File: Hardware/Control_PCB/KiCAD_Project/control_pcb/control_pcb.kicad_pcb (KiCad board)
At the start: 4 copper layers, 82.6 x 76.2 mm, 85 parts, among them J1 Conn_01x02, J2 ISP, J3 Spare 2, J5 Micro_SD_Card_Det, J6 Battery, J7 External Switch, Q1 BSS138, SW1 Freq Select, U1 STM32F103CBT6, U2 SN74LVC1G18, U3 TX2M-400-5-NSSL, U4 IF-D96F, U5 TC4S584F, U6 MAX-M8C, U7 LT1521-3.3, U8 MAX3232, Y1 8MHz

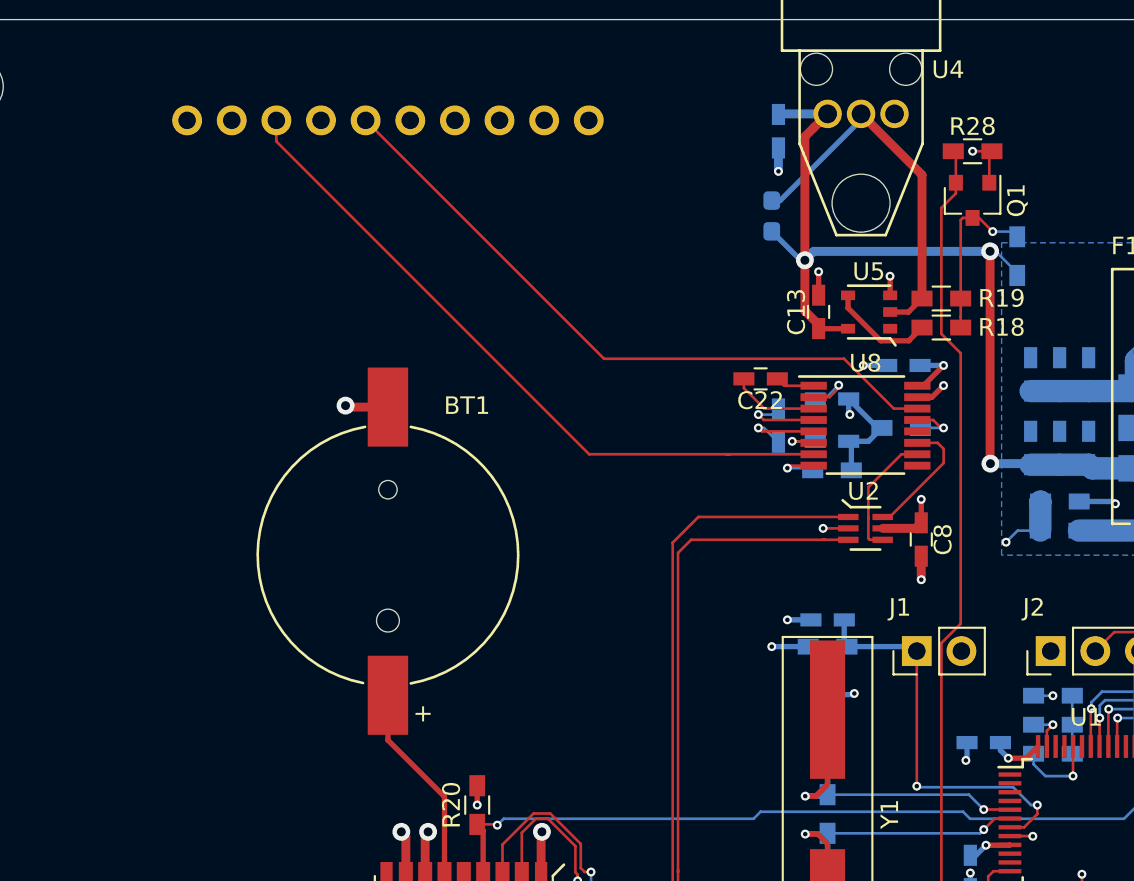
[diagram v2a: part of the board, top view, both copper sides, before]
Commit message: Fix TX2M footprint. Closes #2
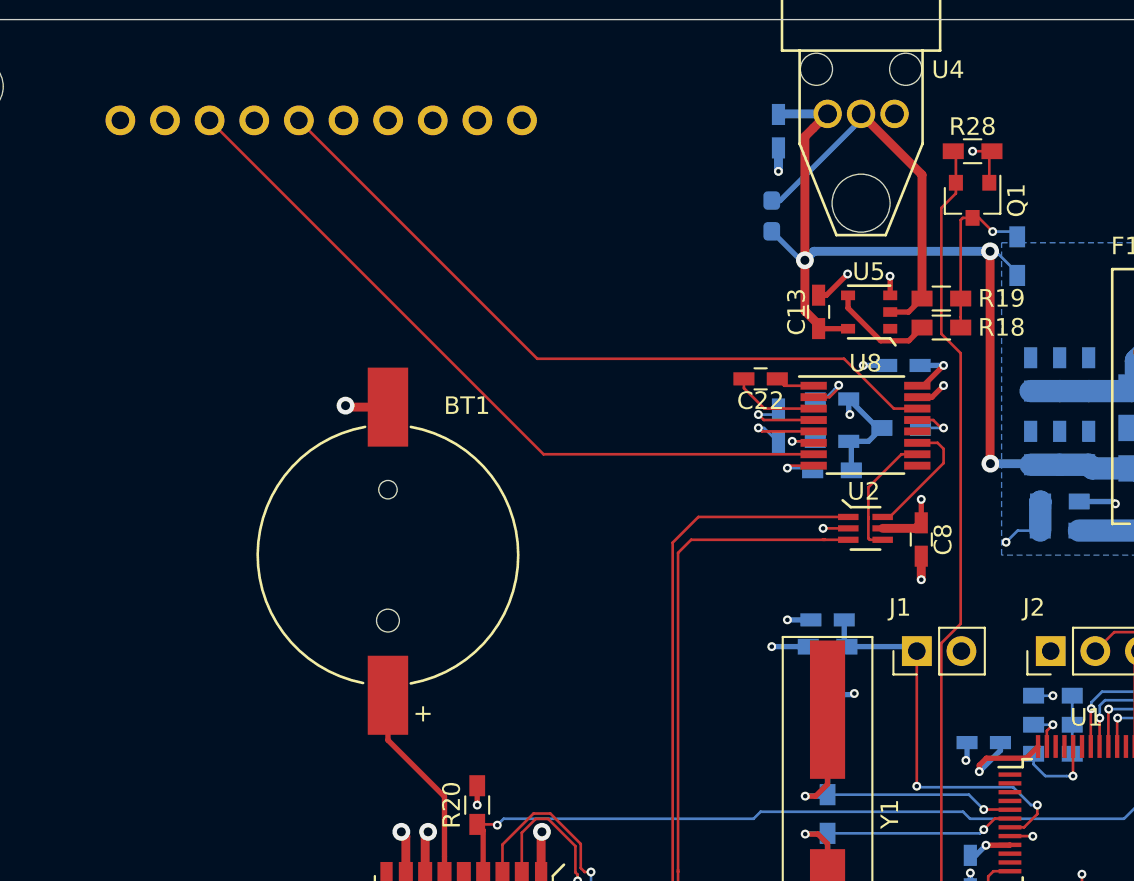
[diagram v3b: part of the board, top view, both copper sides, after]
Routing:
- net /radio/Programming_RS232: track 38.2 -> 42.0 mm
- net +3V3: track 64.8 -> 68.0 mm
- net /radio/Data_RS232: track 39.4 -> 42.2 mm
- net GND: track 66.2 -> 67.0 mm
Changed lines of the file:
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@@
     (thickness 1.6)
     (drawings 8)
-    (tracks 659)
+    (tracks 660)
     (zones 0)
     (modules 85)
@@
     (add_net TX_to_Radio)
   )
+  (module lib_fp:TX2M (layer B.Cu)
+    (at 100.965 128.905 90)
+    (fp_text reference U3 (at 24.257 -20.32 90) (layer B.SilkS)
+      (effects (font (size 1 1) (thickness 0.15)) (justify mirror))
+    )
+    (fp_text value TX2M-400-5-NSSL (at 0 0 90) (layer B.Fab)
+      (effects (font (size 1 1) (thickness 0.15)) (justify mirror))
+    )
+    (fp_line (start -30 -19.5) (end -30 19.5) (layer B.SilkS) (width 0.1))
+    (fp_line (start 30 -19.5) (end -30 -19.5) (layer B.SilkS) (width 0.1))
+    (fp_line (start 30 19.5) (end 30 -19.5) (layer B.SilkS) (width 0.1))
+    (fp_line (start -30 19.5) (end 30 19.5) (layer B.SilkS) (width 0.1))
+    (pad 8C thru_hole circle (at 26.65 -10.15 90) (size 1.7 1.7) (drill 1) (layers *.Cu *.Mask)
+      (net 51 /radio/Data_RS232))
+    (pad 2B thru_hole circle (at -24.11 -16.5 90) (size 1.7 1.7) (drill 1) (layers *.Cu *.Mask)
+      (net 1 "Net-(AE1-Pad1)"))
+    (pad 10C thru_hole circle (at 26.65 -15.23 90) (size 1.7 1.7) (drill 1) (layers *.Cu *.Mask))
+    (pad 9C thru_hole circle (at 26.65 -12.69 90) (size 1.7 1.7) (drill 1) (layers *.Cu *.Mask))
+    (pad 5C thru_hole circle (at 26.65 -2.53 90) (size 1.7 1.7) (drill 1) (layers *.Cu *.Mask))
+    (pad 3B thru_hole circle (at -26.65 -16.5 90) (size 1.7 1.7) (drill 1) (layers *.Cu *.Mask)
+      (net 2 GND))
+    (pad 1B thru_hole circle (at -21.57 -16.5 90) (size 1.7 1.7) (drill 1) (layers *.Cu *.Mask)
+      (net 2 GND))
+    (pad 2A thru_hole circle (at -26.65 16.5 90) (size 1.7 1.7) (drill 1) (layers *.Cu *.Mask)
+      (net 2 GND))
+    (pad 7C thru_hole circle (at 26.65 -7.61 90) (size 1.7 1.7) (drill 1) (layers *.Cu *.Mask)
+      (net 2 GND))
+    (pad 2C thru_hole circle (at 26.65 5.09 90) (size 1.7 1.7) (drill 1) (layers *.Cu *.Mask)
+      (net 2 GND))
+    (pad 1C thru_hole circle (at 26.65 7.63 90) (size 1.7 1.7) (drill 1) (layers *.Cu *.Mask)
+      (net 2 GND))
+    (pad 6C thru_hole circle (at 26.65 -5.07 90) (size 1.7 1.7) (drill 1) (layers *.Cu *.Mask)
+      (net 50 /radio/Programming_RS232))
+    (pad 4C thru_hole circle (at 26.65 0.01 90) (size 1.7 1.7) (drill 1) (layers *.Cu *.Mask))
+    (pad 3C thru_hole circle (at 26.65 2.55 90) (size 1.7 1.7) (drill 1) (layers *.Cu *.Mask))
+    (pad 1A thru_hole circle (at -24.11 16.5 90) (size 1.7 1.7) (drill 1) (layers *.Cu *.Mask)
+      (net 9 +BATT))
+  )
   (module lib_fp:SMA (layer F.Cu)
     (at 87.884 165.735)
@@
       (net 38 Radio_Serial_Select))
   )
-  (module lib_fp:TX2M (layer B.Cu)
-    (at 100.965 128.905 90)
-    (fp_text reference U3 (at 24.257 -20.32 90) (layer B.SilkS)
-      (effects (font (size 1 1) (thickness 0.15)) (justify mirror))
-    )
-    (fp_text value TX2M-400-5-NSSL (at 0 0 90) (layer B.Fab)
-      (effects (font (size 1 1) (thickness 0.15)) (justify mirror))
-    )
-    (fp_line (start -30 19.5) (end 30 19.5) (layer B.SilkS) (width 0.1))
-    (fp_line (start 30 19.5) (end 30 -19.5) (layer B.SilkS) (width 0.1))
-    (fp_line (start 30 -19.5) (end -30 -19.5) (layer B.SilkS) (width 0.1))
-    (fp_line (start -30 -19.5) (end -30 19.5) (layer B.SilkS) (width 0.1))
-    (pad 1A thru_hole circle (at -24.11 16.5 90) (size 1.7 1.7) (drill 1) (layers *.Cu *.Mask)
-      (net 9 +BATT))
-    (pad 3C thru_hole circle (at 26.65 6.35 90) (size 1.7 1.7) (drill 1) (layers *.Cu *.Mask))
-    (pad 4C thru_hole circle (at 26.65 3.81 90) (size 1.7 1.7) (drill 1) (layers *.Cu *.Mask))
-    (pad 6C thru_hole circle (at 26.65 -1.27 90) (size 1.7 1.7) (drill 1) (layers *.Cu *.Mask)
-      (net 50 /radio/Programming_RS232))
-    (pad 1C thru_hole circle (at 26.65 11.43 90) (size 1.7 1.7) (drill 1) (layers *.Cu *.Mask)
-      (net 2 GND))
-    (pad 2C thru_hole circle (at 26.65 8.89 90) (size 1.7 1.7) (drill 1) (layers *.Cu *.Mask)
-      (net 2 GND))
-    (pad 7C thru_hole circle (at 26.65 -3.81 90) (size 1.7 1.7) (drill 1) (layers *.Cu *.Mask)
-      (net 2 GND))
-    (pad 2A thru_hole circle (at -26.65 16.5 90) (size 1.7 1.7) (drill 1) (layers *.Cu *.Mask)
-      (net 2 GND))
-    (pad 1B thru_hole circle (at -21.57 -16.5 90) (size 1.7 1.7) (drill 1) (layers *.Cu *.Mask)
-      (net 2 GND))
-    (pad 3B thru_hole circle (at -26.65 -16.5 90) (size 1.7 1.7) (drill 1) (layers *.Cu *.Mask)
-      (net 2 GND))
-    (pad 5C thru_hole circle (at 26.65 1.27 90) (size 1.7 1.7) (drill 1) (layers *.Cu *.Mask))
-    (pad 9C thru_hole circle (at 26.65 -8.89 90) (size 1.7 1.7) (drill 1) (layers *.Cu *.Mask))
-    (pad 10C thru_hole circle (at 26.65 -11.43 90) (size 1.7 1.7) (drill 1) (layers *.Cu *.Mask))
-    (pad 2B thru_hole circle (at -24.11 -16.5 90) (size 1.7 1.7) (drill 1) (layers *.Cu *.Mask)
-      (net 1 "Net-(AE1-Pad1)"))
-    (pad 8C thru_hole circle (at 26.65 -6.35 90) (size 1.7 1.7) (drill 1) (layers *.Cu *.Mask)
-      (net 51 /radio/Data_RS232))
-  )
   (module lib_fp:IF-D96F (layer F.Cu)
     (at 127.892001 101.887001)
@@
   (segment (start 129.55 112.214001) (end 129.55 111.135) (width 0.3048) (layer F.Cu) (net 2) (status 10))
   (segment (start 129.55 111.135) (end 129.54 111.125) (width 0.3048) (layer F.Cu) (net 2))
-  (via (at 125.476 110.871) (size 0.508) (drill 0.254) (layers F.Cu B.Cu) (net 2))
-  (segment (start 125.476 112.207) (end 125.476 110.871) (width 0.3048) (layer F.Cu) (net 2) (status 10))
   (segment (start 123.19 103.82) (end 123.19 105.156) (width 0.508) (layer B.Cu) (net 2) (status 10))
   (via (at 131.318 128.397) (size 0.508) (drill 0.254) (layers F.Cu B.Cu) (net 2))
@@
   (via (at 125.73 125.476) (size 0.508) (drill 0.254) (layers F.Cu B.Cu) (net 2))
   (segment (start 127.1651 125.476) (end 125.73 125.476) (width 0.1524) (layer F.Cu) (net 2) (status 10))
+  (via (at 127.127 110.998) (size 0.508) (drill 0.254) (layers F.Cu B.Cu) (net 2))
+  (segment (start 125.476 112.207) (end 125.918 112.207) (width 0.3048) (layer F.Cu) (net 2))
+  (segment (start 125.918 112.207) (end 127.127 110.998) (width 0.3048) (layer F.Cu) (net 2))
   (segment (start 100.33 165.735) (end 100.33 159.977) (width 0.34798) (layer F.Cu) (net 3) (status 30))
   (segment (start 101.831 159.977) (end 101.981 159.827) (width 0.34798) (layer F.Cu) (net 3) (status 30))
@@
   (via (at 122.809 132.207) (size 0.508) (drill 0.254) (layers F.Cu B.Cu) (net 8))
   (segment (start 124.884 132.207) (end 122.809 132.207) (width 0.3048) (layer B.Cu) (net 8) (status 10))
-  (via (at 136.271 138.557) (size 0.508) (drill 0.254) (layers F.Cu B.Cu) (net 8))
   (segment (start 135.824 137.668) (end 135.824 138.11) (width 0.3048) (layer B.Cu) (net 8) (status 10))
-  (segment (start 135.824 138.11) (end 136.271 138.557) (width 0.3048) (layer B.Cu) (net 8))
   (segment (start 137.299 138.557) (end 137.966 137.89) (width 0.3048) (layer F.Cu) (net 8) (status 20))
-  (segment (start 136.271 138.557) (end 137.299 138.557) (width 0.3048) (layer F.Cu) (net 8))
   (via (at 139.065 150.114) (size 0.508) (drill 0.254) (layers F.Cu B.Cu) (net 8))
   (segment (start 139.065 148.801) (end 139.065 150.114) (width 0.1524) (layer B.Cu) (net 8) (status 10))
@@
   (via (at 134.239 104.013) (size 0.508) (drill 0.254) (layers F.Cu B.Cu) (net 8))
   (segment (start 135.339 104.013) (end 134.239 104.013) (width 0.1524) (layer F.Cu) (net 8) (status 10))
+  (via (at 134.62 139.319) (size 0.508) (drill 0.254) (layers F.Cu B.Cu) (net 8))
+  (segment (start 135.824 138.11) (end 135.824 138.115) (width 0.3048) (layer B.Cu) (net 8))
+  (segment (start 135.824 138.115) (end 134.62 139.319) (width 0.3048) (layer B.Cu) (net 8))
+  (segment (start 135.02279 138.557) (end 137.299 138.557) (width 0.3048) (layer F.Cu) (net 8))
+  (segment (start 134.62 138.95979) (end 135.02279 138.557) (width 0.3048) (layer F.Cu) (net 8))
+  (segment (start 134.62 139.319) (end 134.62 138.95979) (width 0.3048) (layer F.Cu) (net 8))
   (segment (start 125.483001 114.114001) (end 125.476 114.107) (width 0.3048) (layer F.Cu) (net 9) (status 30))
   (segment (start 127.15 114.114001) (end 125.483001 114.114001) (width 0.3048) (layer F.Cu) (net 9) (status 30))
@@
   (segment (start 125.011 122.047) (end 125.138 122.174) (width 0.1524) (layer B.Cu) (net 49) (status 30))
   (segment (start 123.698 122.047) (end 125.011 122.047) (width 0.1524) (layer B.Cu) (net 49) (status 20))
-  (segment (start 131.093 118.659) (end 129.75575 118.659) (width 0.1524) (layer F.Cu) (net 50) (status 10))
+  (segment (start 126.92075 115.824) (end 109.464 115.824) (width 0.1524) (layer F.Cu) (net 50))
+  (segment (start 109.464 115.824) (end 95.895 102.255) (width 0.1524) (layer F.Cu) (net 50))
+  (segment (start 131.093 118.659) (end 129.75575 118.659) (width 0.1524) (layer F.Cu) (net 50))
   (segment (start 129.75575 118.659) (end 126.92075 115.824) (width 0.1524) (layer F.Cu) (net 50))
-  (segment (start 113.264 115.824) (end 99.695 102.255) (width 0.1524) (layer F.Cu) (net 50) (status 20))
-  (segment (start 126.92075 115.824) (end 113.264 115.824) (width 0.1524) (layer F.Cu) (net 50))
-  (segment (start 112.416919 121.259) (end 120.422 121.259) (width 0.1524) (layer F.Cu) (net 51))
-  (segment (start 94.615 103.457081) (end 112.416919 121.259) (width 0.1524) (layer F.Cu) (net 51))
-  (segment (start 94.615 102.255) (end 94.615 103.457081) (width 0.1524) (layer F.Cu) (net 51) (status 10))
-  (segment (start 125.193 121.259) (end 120.422 121.259) (width 0.1524) (layer F.Cu) (net 51) (status 10))
-  (segment (start 120.422 121.259) (end 120.223 121.259) (width 0.1524) (layer F.Cu) (net 51))
+  (segment (start 109.819 121.259) (end 125.193 121.259) (width 0.1524) (layer F.Cu) (net 51))
+  (segment (start 90.815 102.255) (end 109.819 121.259) (width 0.1524) (layer F.Cu) (net 51))
   (segment (start 145.066 144.49) (end 149.737468 144.49) (width 0.1524) (layer F.Cu) (net 52) (status 10))
   (segment (start 141.732 154.432) (end 141.732 155.697) (width 0.1524) (layer F.Cu) (net 52) (status 20))

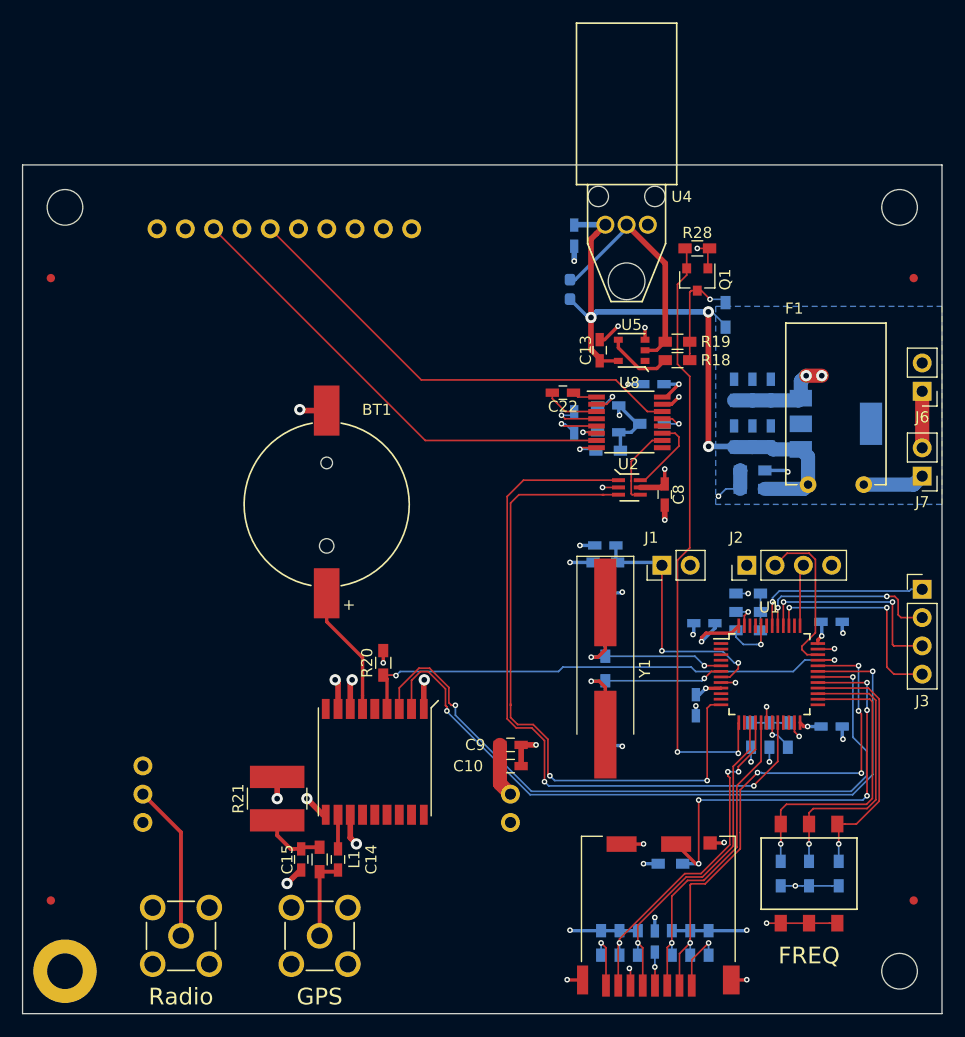
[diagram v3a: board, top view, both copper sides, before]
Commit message: Change UARTS for separate radio serial.
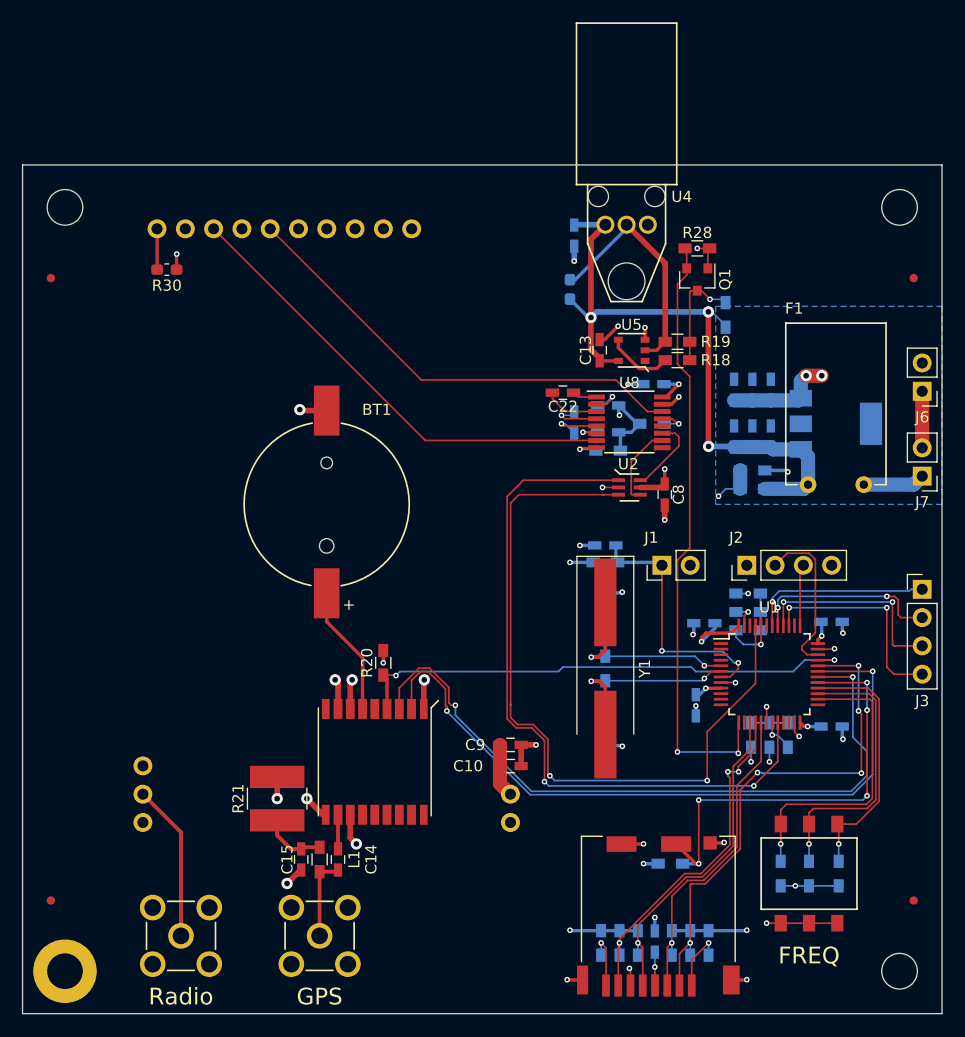
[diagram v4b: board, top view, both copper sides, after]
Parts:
- added R30: NP, Resistor_SMD:R_0603_1608Metric_Pad1.05x0.95mm_HandSolder, F.Cu at (86.6, 105.9)
- J3: value Spare 2 -> Spare
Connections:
- U1 pad 12: TX_to_Radio -> (no net)
- U1 pad 45: (no net) -> TX_to_Radio
- U3 pad 10C: (no net) -> Net-(R30-Pad2)
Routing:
- net TX_to_Radio: track 59.2 -> 67.0 mm
- net Net-(R30-Pad2): track 0.00 -> 3.66 mm
- net GND: track 67.0 -> 68.4 mm, vias 34 -> 35
